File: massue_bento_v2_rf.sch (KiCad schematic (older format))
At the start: 0 parts

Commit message: Add: RF / CC3000 schematic section based upon reference design
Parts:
- added A?: 2500AT44M0400, symbol ANT
- added C? (x2): C, symbol C
- added C?: 10pF, symbol C
- added C?: 2.2pF, symbol C
- added L?: 2.2nH, symbol INDUCTOR
- added L?: NC, symbol INDUCTOR
- added P? (x5): TST, symbol TST
- added R?: OR, symbol R
- added R?: NC, symbol R
- added U?: CC3000, symbol CC3000
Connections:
- new net: P?.1, U?.2 (RESERVED_1)
- new net: P?.1, U?.24 (RESERVED_3)
- new net: U?.27 (SDA_EEPROM), U?.28 (SDA_CC3000)
- new net: U?.28 (SDA_CC3000), U?.29 (SCL_EEPROM)
- new net: C?.2, U?.35 (RF_ANT)
- new net: P?.1, U?.4 (RESERVED_2)
- new net: P?.1, U?.6 (WL_RS232_TX)
- new net: P?.1, U?.8 (WL_RS232_RX)
- new net: C?.1, C?.1, L?.1
- new net: A?.1, C?.2, L?.1
- new net +3.3V: C?.1, C?.1, U?.19 (VBAT_IN), U?.23 (VIO_HOST)
- new net CC3000_SPI_CLK: U?.17 (SPI_CLK)
- new net CC3000_SPI_CS: U?.12 (SPI_CS)
- new net CC3000_SPI_DIN: U?.15 (SPI_DIN)
- new net CC3000_SPI_DOUT: U?.13 (SPI_DOUT)
- new net CC3000_SPI_IRQ: U?.14 (SPI_IRQ)
- new net CC3000_SW_EN: U?.26 (VBAT_SW_EN)
- new net GND: C?.2, C?.2, R?.2, U?.1 (GND), U?.10 (GND), U?.11 (GND), U?.16 (GND), U?.18 (GND), U?.20 (GND), U?.21 (EXT_32K), U?.22 (GND), U?.25 (GND), U?.31 (GND), U?.32 (GND), U?.33 (GND), U?.34 (GND), U?.36 (GND), U?.37 (GND), U?.38 (GND), U?.39 (GND), U?.40 (GND), U?.41 (GND), U?.42 (GND), U?.43 (GND), U?.44 (GND), U?.46 (GND), U?.9 (GND)
- new net WL_EN1: R?.1, U?.7 (WL_EN1)
- new net WL_EN2: R?.1, R?.2, U?.5 (WL_EN2)

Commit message: Fix: use battery voltage to power CC3000
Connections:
- net +3.3V: no longer C?.1, U?.19 (VBAT_IN)
- new net VBAT: C?.1, U?.19 (VBAT_IN)
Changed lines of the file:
@@
 LIBS:valves
 LIBS:tom_kicad
+LIBS:massue_bento_v2_rf-cache
 EELAYER 24 0
 EELAYER END
@@
 Wire Wire Line
 	7350 4250 7350 4350
-$Comp
-L +3.3V #PWR010
-U 1 1 53A588D9
-P 7350 4250
-F 0 "#PWR010" H 7350 4210 30  0001 C CNN
-F 1 "+3.3V" H 7350 4360 30  0000 C CNN
-F 2 "" H 7350 4250 60  0000 C CNN
-F 3 "" H 7350 4250 60  0000 C CNN
-	1    7350 4250
-	1    0    0    -1
-$EndComp
 Connection ~ 7350 4300
 $Comp
@@
 Wire Wire Line
 	2550 1600 2550 1450
+$Comp
+L VBAT #PWR?
+U 1 1 53A58531
+P 7350 4250
+F 0 "#PWR?" H 7350 4310 30  0001 C CNN
+F 1 "VBAT" H 7350 4360 30  0000 C CNN
+F 2 "" H 7350 4250 60  0000 C CNN
+F 3 "" H 7350 4250 60  0000 C CNN
+	1    7350 4250
+	1    0    0    -1
+$EndComp
 $EndSCHEMATC

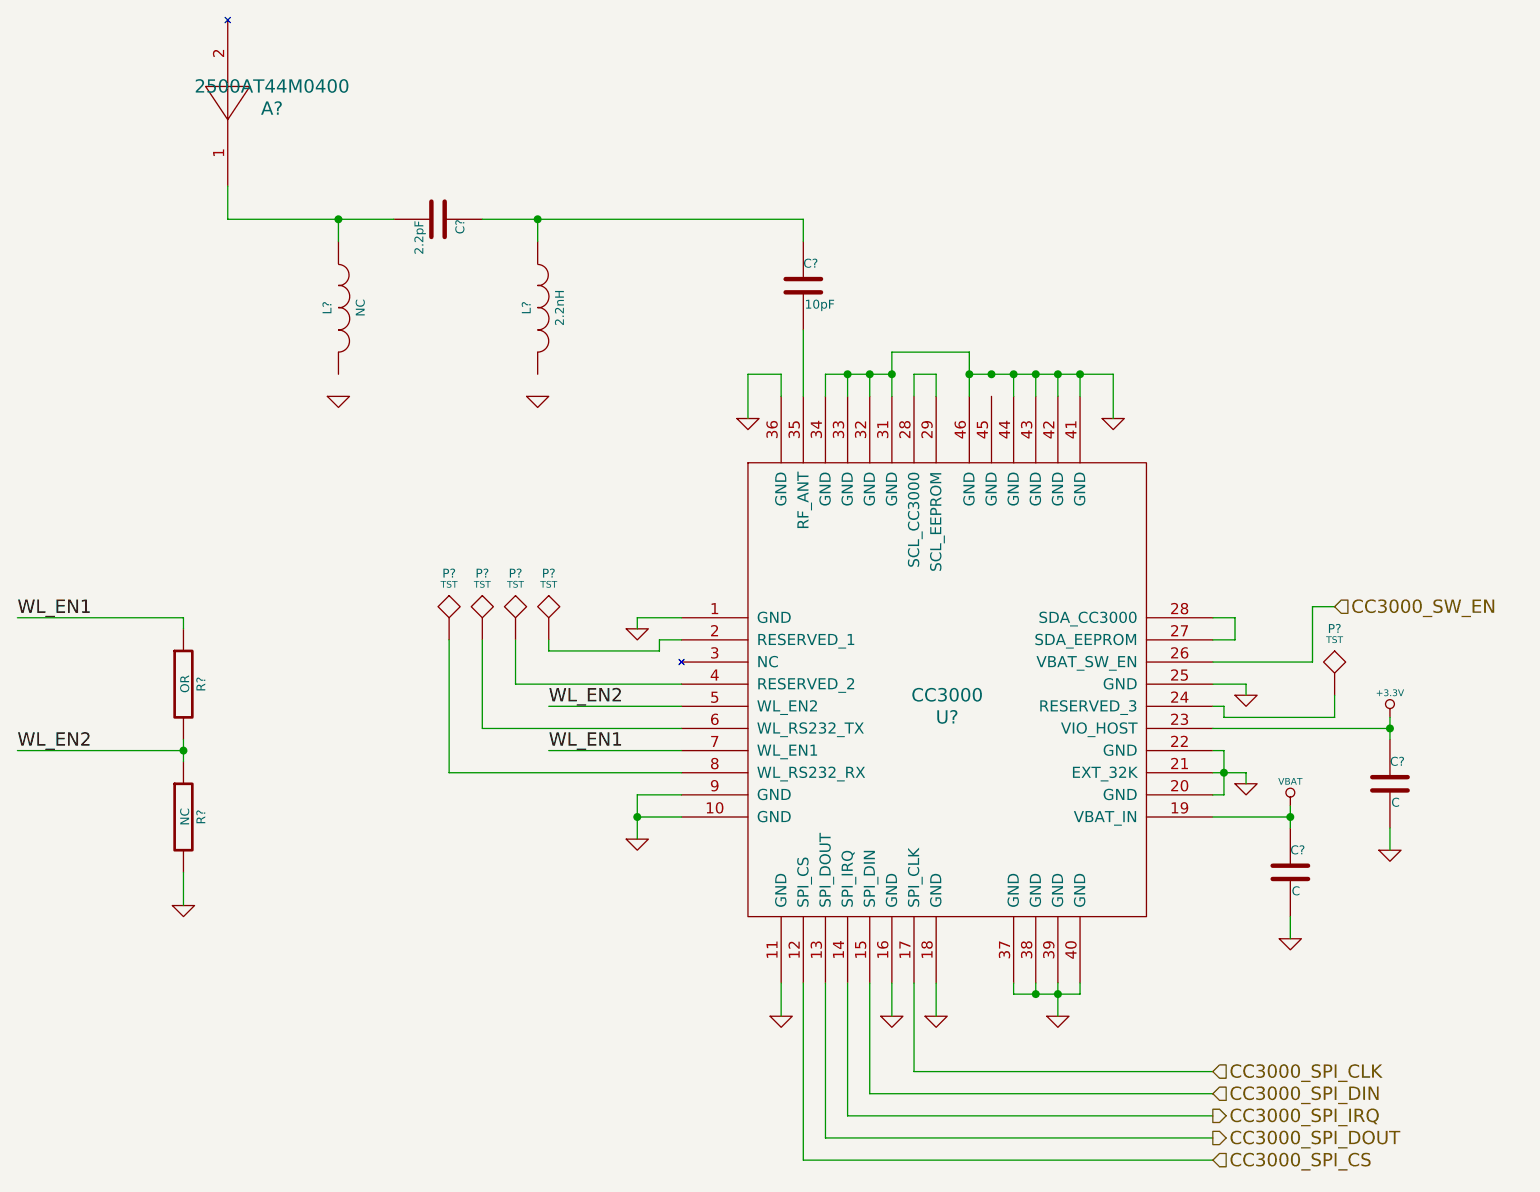
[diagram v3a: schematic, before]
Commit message: Fix: global annotation, fixed bugs to satisfy ERC
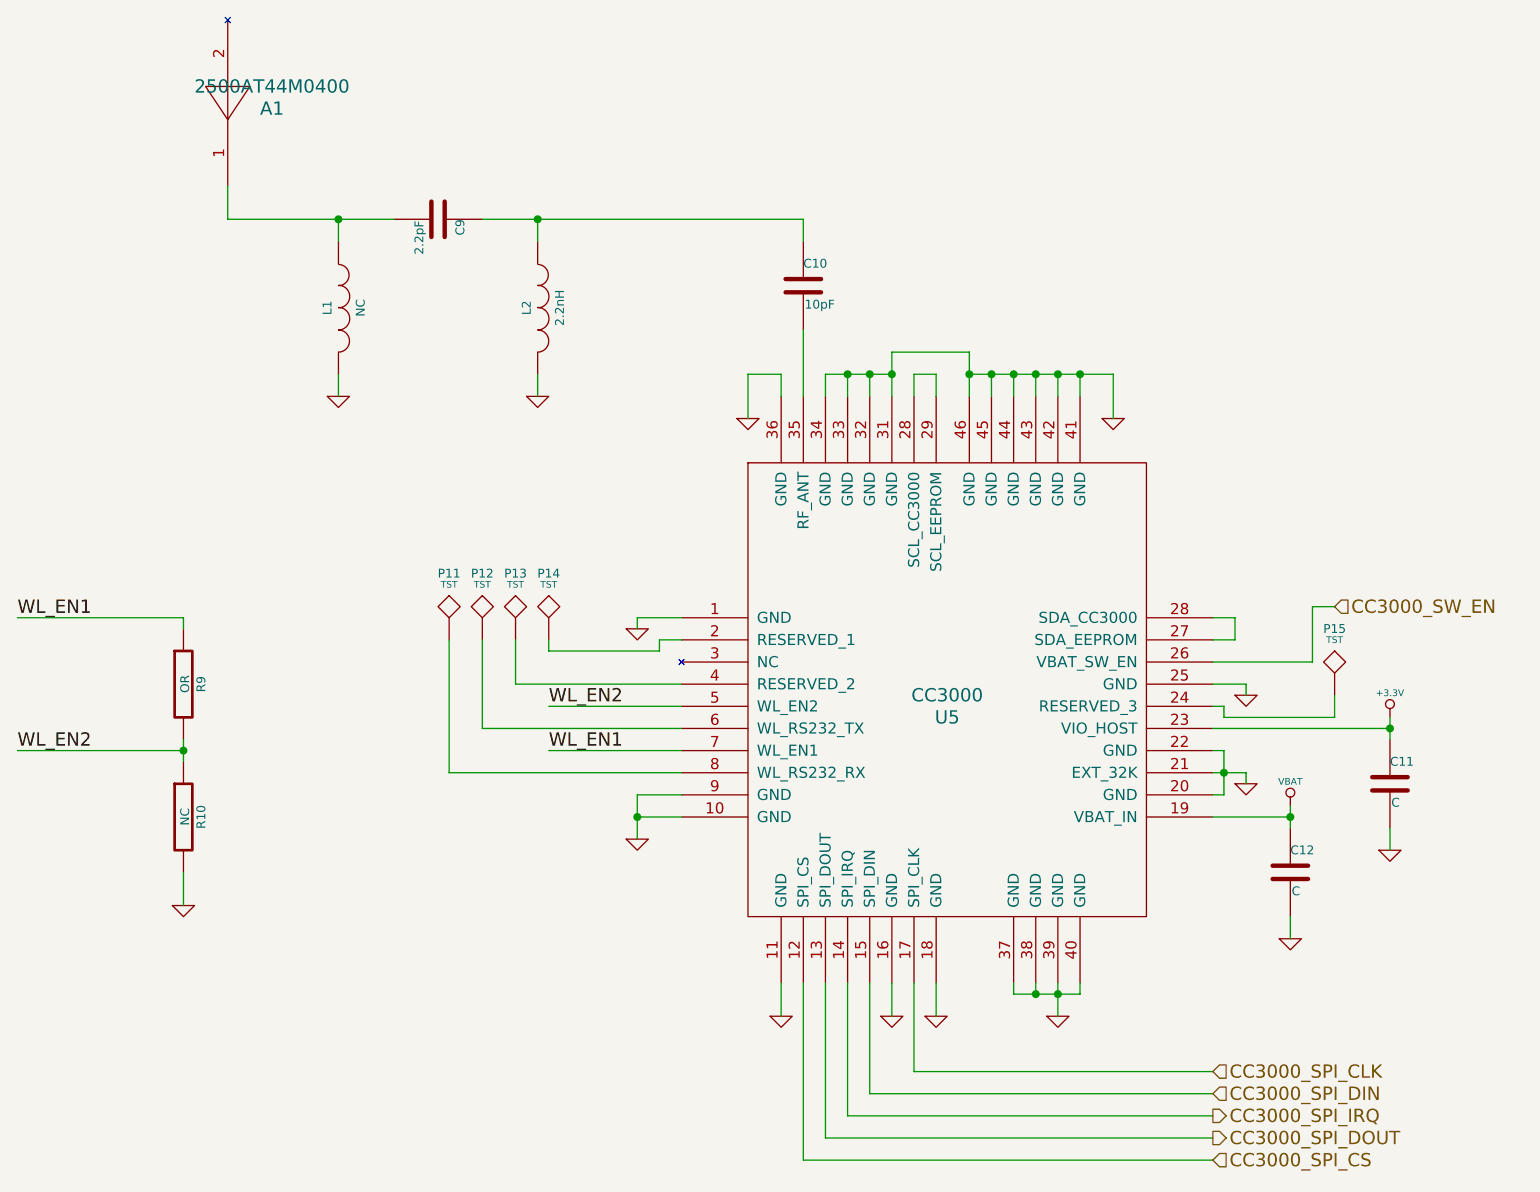
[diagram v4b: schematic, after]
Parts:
- gave numbers to parts that had none: 15
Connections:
- net GND: now also L1.2, L2.2, U5.45 (GND)
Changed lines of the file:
@@
 $EndDescr
 $Comp
-L CC3000 U?
+L CC3000 U5
 U 1 1 53A5775B
 P 5550 4100
-F 0 "U?" H 5800 4350 60  0000 C CNN
+F 0 "U5" H 5800 4350 60  0000 C CNN
 F 1 "CC3000" H 5800 4450 60  0000 C CNN
 F 2 "" H 5800 4450 60  0000 C CNN
@@
 $EndComp
 $Comp
-L GND #PWR01
+L GND #PWR040
 U 1 1 53A57B5B
 P 4400 3450
-F 0 "#PWR01" H 4400 3450 30  0001 C CNN
+F 0 "#PWR040" H 4400 3450 30  0001 C CNN
 F 1 "GND" H 4400 3380 30  0001 C CNN
 F 2 "" H 4400 3450 60  0000 C CNN
@@
 	4000 3550 4000 3500
 $Comp
-L TST P?
+L TST P14
 U 1 1 53A57B90
 P 4000 3500
-F 0 "P?" H 4000 3800 40  0000 C CNN
+F 0 "P14" H 4000 3800 40  0000 C CNN
 F 1 "TST" H 4000 3750 30  0000 C CNN
 F 2 "" H 4000 3500 60  0000 C CNN
@@
 $EndComp
 $Comp
-L TST P?
+L TST P13
 U 1 1 53A57BE6
 P 3850 3500
-F 0 "P?" H 3850 3800 40  0000 C CNN
+F 0 "P13" H 3850 3800 40  0000 C CNN
 F 1 "TST" H 3850 3750 30  0000 C CNN
 F 2 "" H 3850 3500 60  0000 C CNN
@@
 $EndComp
 $Comp
-L TST P?
+L TST P12
 U 1 1 53A57C03
 P 3700 3500
-F 0 "P?" H 3700 3800 40  0000 C CNN
+F 0 "P12" H 3700 3800 40  0000 C CNN
 F 1 "TST" H 3700 3750 30  0000 C CNN
 F 2 "" H 3700 3500 60  0000 C CNN
@@
 $EndComp
 $Comp
-L TST P?
+L TST P11
 U 1 1 53A57C1D
 P 3550 3500
-F 0 "P?" H 3550 3800 40  0000 C CNN
+F 0 "P11" H 3550 3800 40  0000 C CNN
 F 1 "TST" H 3550 3750 30  0000 C CNN
 F 2 "" H 3550 3500 60  0000 C CNN
@@
 WL_EN1
 $Comp
-L R R?
+L R R9
 U 1 1 53A57D13
 P 2350 3700
-F 0 "R?" V 2430 3700 40  0000 C CNN
+F 0 "R9" V 2430 3700 40  0000 C CNN
 F 1 "OR" V 2357 3701 40  0000 C CNN
 F 2 "" V 2280 3700 30  0000 C CNN
@@
 $EndComp
 $Comp
-L R R?
+L R R10
 U 1 1 53A57D82
 P 2350 4300
-F 0 "R?" V 2430 4300 40  0000 C CNN
+F 0 "R10" V 2430 4300 40  0000 C CNN
 F 1 "NC" V 2357 4301 40  0000 C CNN
 F 2 "" V 2280 4300 30  0000 C CNN
@@
 $EndComp
 $Comp
-L GND #PWR02
+L GND #PWR041
 U 1 1 53A57DBF
 P 2350 4700
-F 0 "#PWR02" H 2350 4700 30  0001 C CNN
+F 0 "#PWR041" H 2350 4700 30  0001 C CNN
 F 1 "GND" H 2350 4630 30  0001 C CNN
 F 2 "" H 2350 4700 60  0000 C CNN
@@
 WL_EN2
 $Comp
-L GND #PWR03
+L GND #PWR042
 U 1 1 53A57EDD
 P 4400 4400
-F 0 "#PWR03" H 4400 4400 30  0001 C CNN
+F 0 "#PWR042" H 4400 4400 30  0001 C CNN
 F 1 "GND" H 4400 4330 30  0001 C CNN
 F 2 "" H 4400 4400 60  0000 C CNN
@@
 Connection ~ 4400 4300
 $Comp
-L GND #PWR04
+L GND #PWR043
 U 1 1 53A57FA7
 P 5050 5200
-F 0 "#PWR04" H 5050 5200 30  0001 C CNN
+F 0 "#PWR043" H 5050 5200 30  0001 C CNN
 F 1 "GND" H 5050 5130 30  0001 C CNN
 F 2 "" H 5050 5200 60  0000 C CNN
@@
 $EndComp
 $Comp
-L GND #PWR05
+L GND #PWR044
 U 1 1 53A57FB9
 P 5750 5200
-F 0 "#PWR05" H 5750 5200 30  0001 C CNN
+F 0 "#PWR044" H 5750 5200 30  0001 C CNN
 F 1 "GND" H 5750 5130 30  0001 C CNN
 F 2 "" H 5750 5200 60  0000 C CNN
@@
 $EndComp
 $Comp
-L GND #PWR06
+L GND #PWR045
 U 1 1 53A57FCB
 P 6300 5200
-F 0 "#PWR06" H 6300 5200 30  0001 C CNN
+F 0 "#PWR045" H 6300 5200 30  0001 C CNN
 F 1 "GND" H 6300 5130 30  0001 C CNN
 F 2 "" H 6300 5200 60  0000 C CNN
@@
 	5550 5050 5550 5200
 $Comp
-L GND #PWR07
+L GND #PWR046
 U 1 1 53A58109
 P 5550 5200
-F 0 "#PWR07" H 5550 5200 30  0001 C CNN
+F 0 "#PWR046" H 5550 5200 30  0001 C CNN
 F 1 "GND" H 5550 5130 30  0001 C CNN
 F 2 "" H 5550 5200 60  0000 C CNN
@@
 CC3000_SPI_CS
 $Comp
-L GND #PWR08
+L GND #PWR047
 U 1 1 53A5852D
 P 7150 4150
-F 0 "#PWR08" H 7150 4150 30  0001 C CNN
+F 0 "#PWR047" H 7150 4150 30  0001 C CNN
 F 1 "GND" H 7150 4080 30  0001 C CNN
 F 2 "" H 7150 4150 60  0000 C CNN
@@
 	7150 4100 7150 4150
 $Comp
-L C C?
+L C C12
 U 1 1 53A587B8
 P 7350 4550
-F 0 "C?" H 7350 4650 40  0000 L CNN
+F 0 "C12" H 7350 4650 40  0000 L CNN
 F 1 "C" H 7356 4465 40  0000 L CNN
 F 2 "" H 7388 4400 30  0000 C CNN
@@
 $EndComp
 $Comp
-L GND #PWR09
+L GND #PWR048
 U 1 1 53A58837
 P 7350 4850
-F 0 "#PWR09" H 7350 4850 30  0001 C CNN
+F 0 "#PWR048" H 7350 4850 30  0001 C CNN
 F 1 "GND" H 7350 4780 30  0001 C CNN
 F 2 "" H 7350 4850 60  0000 C CNN
@@
 Connection ~ 7350 4300
 $Comp
-L C C?
+L C C11
 U 1 1 53A58B62
 P 7800 4150
-F 0 "C?" H 7800 4250 40  0000 L CNN
+F 0 "C11" H 7800 4250 40  0000 L CNN
 F 1 "C" H 7806 4065 40  0000 L CNN
 F 2 "" H 7838 4000 30  0000 C CNN
@@
 $EndComp
 $Comp
-L GND #PWR011
+L GND #PWR049
 U 1 1 53A58B68
 P 7800 4450
-F 0 "#PWR011" H 7800 4450 30  0001 C CNN
+F 0 "#PWR049" H 7800 4450 30  0001 C CNN
 F 1 "GND" H 7800 4380 30  0001 C CNN
 F 2 "" H 7800 4450 60  0000 C CNN
@@
 	7800 3850 7800 3950
 $Comp
-L +3.3V #PWR012
+L +3.3V #PWR050
 U 1 1 53A58B71
 P 7800 3850
-F 0 "#PWR012" H 7800 3810 30  0001 C CNN
+F 0 "#PWR050" H 7800 3810 30  0001 C CNN
 F 1 "+3.3V" H 7800 3960 30  0000 C CNN
 F 2 "" H 7800 3850 60  0000 C CNN
@@
 Connection ~ 7800 3900
 $Comp
-L TST P?
+L TST P15
 U 1 1 53A58DA7
 P 7550 3750
-F 0 "P?" H 7550 4050 40  0000 C CNN
+F 0 "P15" H 7550 4050 40  0000 C CNN
 F 1 "TST" H 7550 4000 30  0000 C CNN
 F 2 "" H 7550 3750 60  0000 C CNN
@@
 	7550 3750 7550 3850
 $Comp
-L GND #PWR013
+L GND #PWR051
 U 1 1 53A58F4A
 P 7150 3750
-F 0 "#PWR013" H 7150 3750 30  0001 C CNN
+F 0 "#PWR051" H 7150 3750 30  0001 C CNN
 F 1 "GND" H 7150 3680 30  0001 C CNN
 F 2 "" H 7150 3750 60  0000 C CNN
@@
 	5750 2300 5750 2400
 $Comp
-L GND #PWR014
+L GND #PWR052
 U 1 1 53A5961E
 P 6550 2500
-F 0 "#PWR014" H 6550 2500 30  0001 C CNN
+F 0 "#PWR052" H 6550 2500 30  0001 C CNN
 F 1 "GND" H 6550 2430 30  0001 C CNN
 F 2 "" H 6550 2500 60  0000 C CNN
@@
 Connection ~ 6400 2300
 $Comp
-L GND #PWR015
+L GND #PWR053
 U 1 1 53A59CEE
 P 4900 2500
-F 0 "#PWR015" H 4900 2500 30  0001 C CNN
+F 0 "#PWR053" H 4900 2500 30  0001 C CNN
 F 1 "GND" H 4900 2430 30  0001 C CNN
 F 2 "" H 4900 2500 60  0000 C CNN
@@
 Connection ~ 5900 2300
 $Comp
-L C C?
+L C C10
 U 1 1 53A5A0D0
 P 5150 1900
-F 0 "C?" H 5150 2000 40  0000 L CNN
+F 0 "C10" H 5150 2000 40  0000 L CNN
 F 1 "10pF" H 5156 1815 40  0000 L CNN
 F 2 "" H 5188 1750 30  0000 C CNN
@@
 	5150 2400 5150 2100
 $Comp
-L INDUCTOR L?
+L INDUCTOR L2
 U 1 1 53A5A27C
 P 3950 2000
-F 0 "L?" V 3900 2000 40  0000 C CNN
+F 0 "L2" V 3900 2000 40  0000 C CNN
 F 1 "2.2nH" V 4050 2000 40  0000 C CNN
 F 2 "" H 3950 2000 60  0000 C CNN
@@
 $EndComp
 $Comp
-L C C?
+L C C9
 U 1 1 53A5A2E7
 P 3500 1600
-F 0 "C?" H 3500 1700 40  0000 L CNN
+F 0 "C9" H 3500 1700 40  0000 L CNN
 F 1 "2.2pF" H 3506 1515 40  0000 L CNN
 F 2 "" H 3538 1450 30  0000 C CNN
@@
 $EndComp
 $Comp
-L INDUCTOR L?
+L INDUCTOR L1
 U 1 1 53A5A385
 P 3050 2000
-F 0 "L?" V 3000 2000 40  0000 C CNN
+F 0 "L1" V 3000 2000 40  0000 C CNN
 F 1 "NC" V 3150 2000 40  0000 C CNN
 F 2 "" H 3050 2000 60  0000 C CNN
@@
 $EndComp
 $Comp
-L GND #PWR016
+L GND #PWR054
 U 1 1 53A5A40B
 P 3950 2400
-F 0 "#PWR016" H 3950 2400 30  0001 C CNN
+F 0 "#PWR054" H 3950 2400 30  0001 C CNN
 F 1 "GND" H 3950 2330 30  0001 C CNN
 F 2 "" H 3950 2400 60  0000 C CNN
@@
 $EndComp
 $Comp
-L GND #PWR017
+L GND #PWR055
 U 1 1 53A5A45C
 P 3050 2400
-F 0 "#PWR017" H 3050 2400 30  0001 C CNN
+F 0 "#PWR055" H 3050 2400 30  0001 C CNN
 F 1 "GND" H 3050 2330 30  0001 C CNN
 F 2 "" H 3050 2400 60  0000 C CNN
@@
 	3050 1600 3050 1700
 $Comp
-L ANT A?
+L ANT A1
 U 1 1 53A5A6B5
 P 2550 1150
-F 0 "A?" H 2750 1200 60  0000 C CNN
+F 0 "A1" H 2750 1200 60  0000 C CNN
 F 1 "2500AT44M0400" H 2750 1300 60  0000 C CNN
 F 2 "" H 2550 1150 60  0000 C CNN
@@
 	2550 1600 2550 1450
 $Comp
-L VBAT #PWR?
+L VBAT #PWR056
 U 1 1 53A58531
 P 7350 4250
-F 0 "#PWR?" H 7350 4310 30  0001 C CNN
+F 0 "#PWR056" H 7350 4310 30  0001 C CNN
 F 1 "VBAT" H 7350 4360 30  0000 C CNN
 F 2 "" H 7350 4250 60  0000 C CNN
@@
 	1    0    0    -1
 $EndComp
+Wire Wire Line
+	3950 2400 3950 2300
+Wire Wire Line
+	3050 2400 3050 2300
+Wire Wire Line
+	6000 2400 6000 2300
 $EndSCHEMATC
